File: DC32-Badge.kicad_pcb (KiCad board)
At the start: 2 copper layers, 152.4 x 101.6 mm, 55 parts, among them J1 Conn_01x06, J2 Hirose_FH34-SRJ-24S, J3 Conn_01x06, J4 Conn_01x06, J5 Conn_01x06, J6 Micro_SD_Card_Det, P1 2479, Q1 RTF025N03TL, SW1 SW_Push_DPDT, SW2 EVIL_SWITCH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

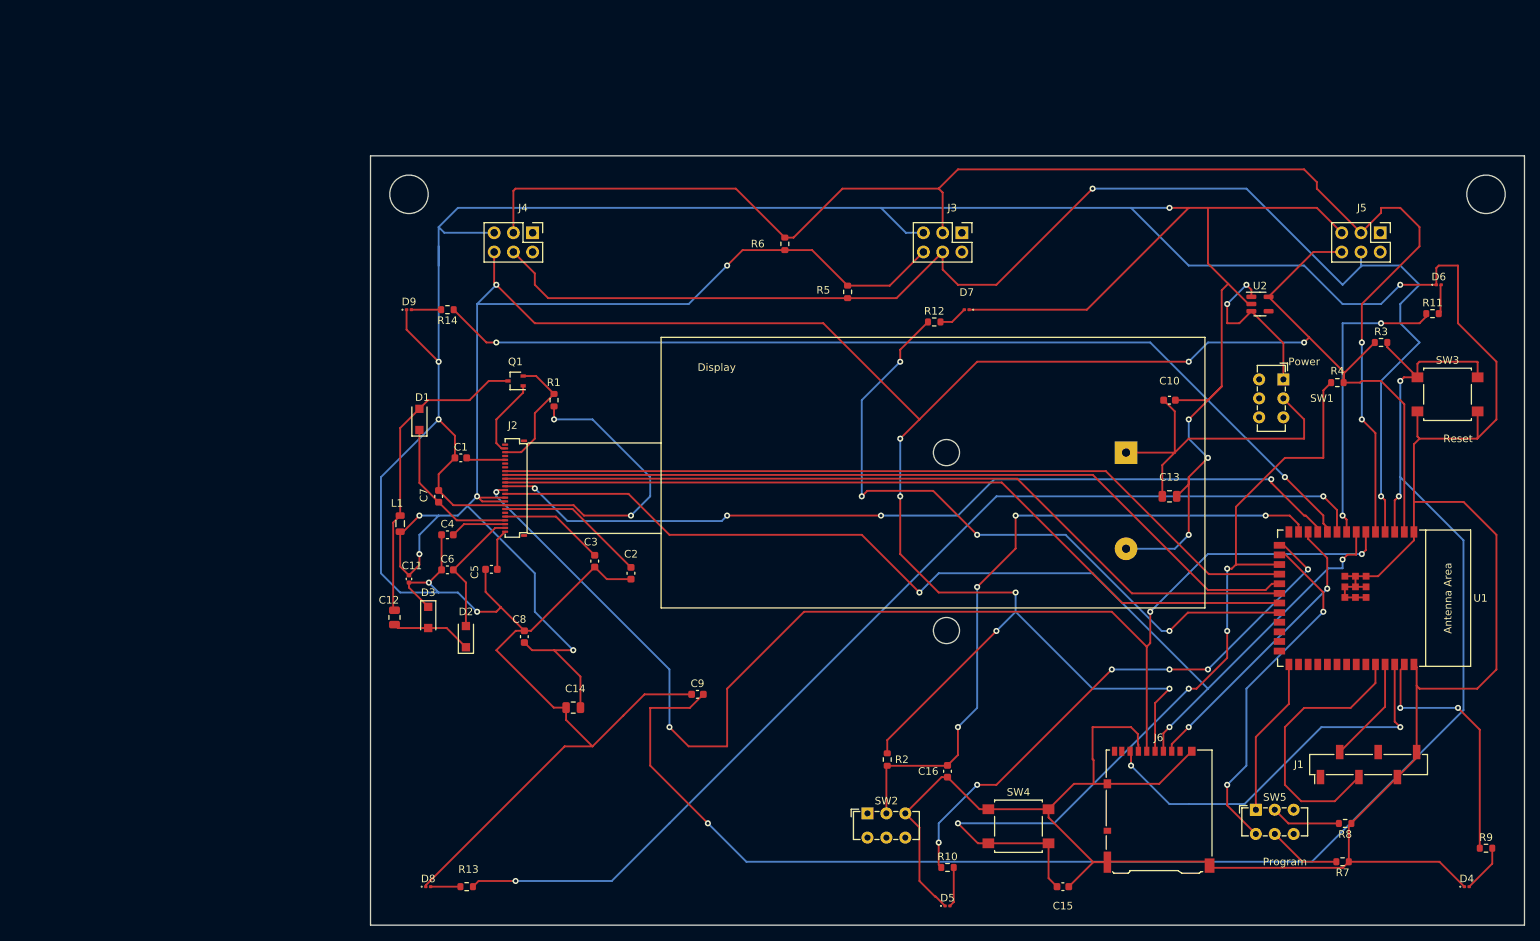
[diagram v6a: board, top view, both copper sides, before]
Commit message: Updated silkscreen.
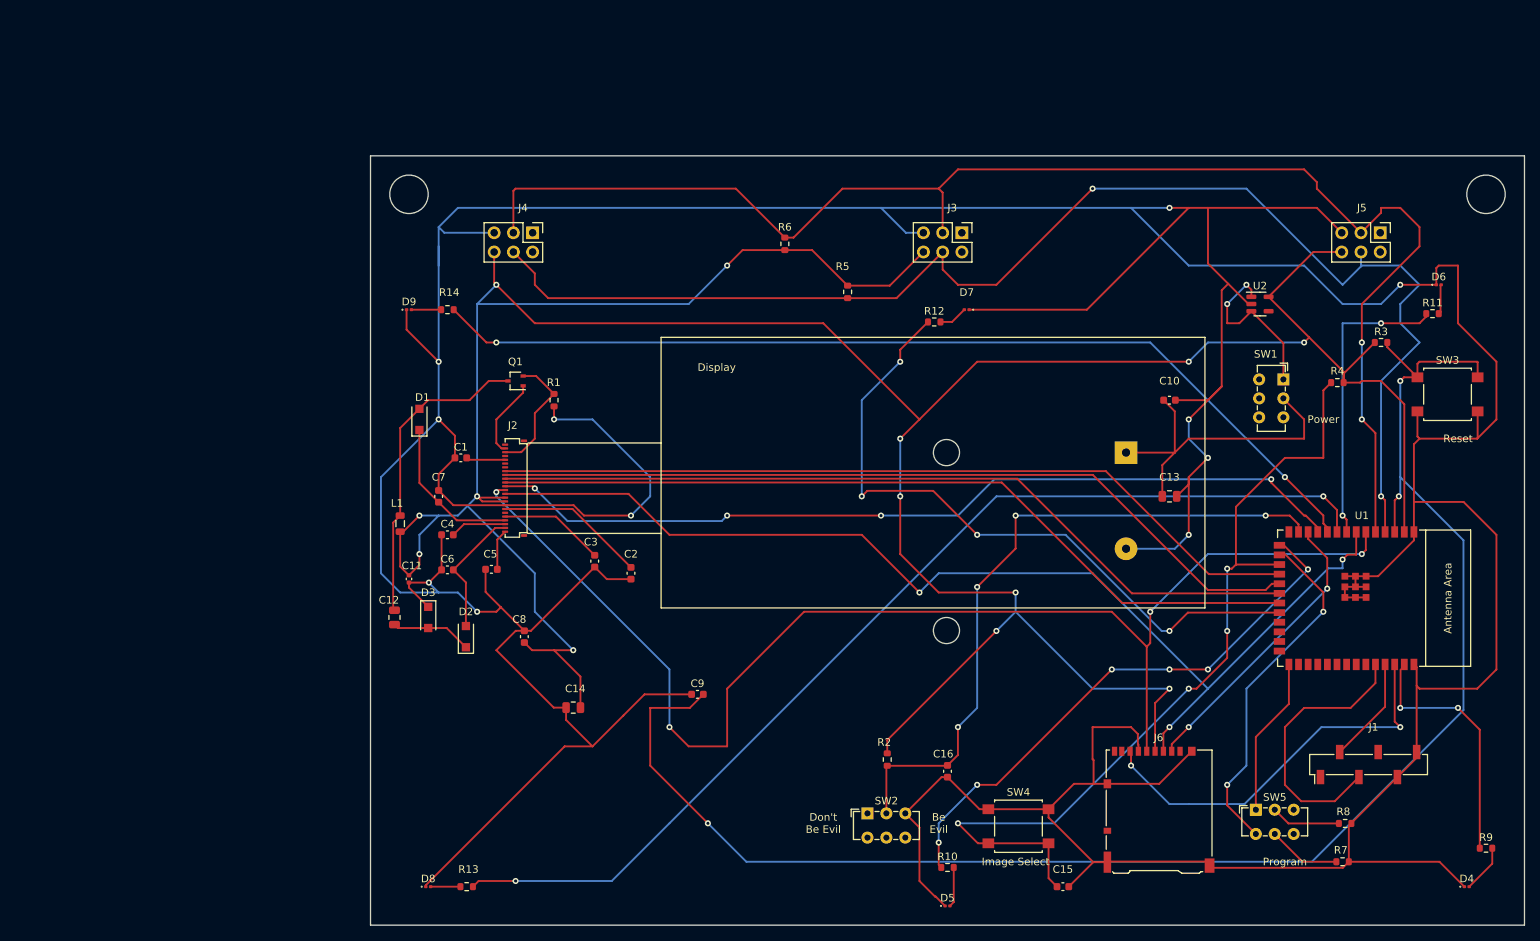
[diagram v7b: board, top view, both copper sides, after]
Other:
- board text added: "Be Evil"
- board text added: "Don't Be Evil"
- board text added: "Image Select"
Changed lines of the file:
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@@
     (property "Sheetname" "")
     (attr smd)
-    (fp_text reference "R7" (at 0 -1.43) (layer "F.SilkS")
+    (fp_text reference "R7" (at 0.237258 1.54) (layer "F.SilkS")
       (effects (font (size 1 1) (thickness 0.15)))
     )
@@
     (property "Sheetname" "")
     (attr smd)
-    (fp_text reference "R5" (at -0.237258 3.21) (layer "F.SilkS")
+    (fp_text reference "R5" (at -3.36 0.67) (layer "F.SilkS")
       (effects (font (size 1 1) (thickness 0.15)))
     )
@@
     (property "Sheetname" "")
     (attr smd)
-    (fp_text reference "C5" (at -2.22 0.35129 90) (layer "F.SilkS")
+    (fp_text reference "C5" (at -0.14058 -2.02 180) (layer "F.SilkS")
       (effects (font (size 1 1) (thickness 0.15)))
     )
@@
     (property "Sheetname" "")
     (attr smd)
-    (fp_text reference "C16" (at 0 -2.54 180) (layer "F.SilkS")
+    (fp_text reference "C16" (at 2.29 -0.56129 180) (layer "F.SilkS")
       (effects (font (size 1 1) (thickness 0.15)))
     )
@@
     (property "Sheetname" "")
     (attr through_hole)
-    (fp_text reference "SW1" (at 2.5 -5.08 180) (layer "F.SilkS")
+    (fp_text reference "SW1" (at -3.34 2.34129 180) (layer "F.SilkS")
       (effects (font (size 1 1) (thickness 0.15)))
     )
@@
     (property "Sheetname" "")
     (attr smd)
-    (fp_text reference "R6" (at 0 -3.577258) (layer "F.SilkS")
+    (fp_text reference "R6" (at 2.214516 0) (layer "F.SilkS")
       (effects (font (size 1 1) (thickness 0.15)))
     )
@@
     (property "Sheetname" "")
     (attr smd)
-    (fp_text reference "C15" (at 0 -2.54) (layer "F.SilkS")
+    (fp_text reference "C15" (at 0 2.29) (layer "F.SilkS")
       (effects (font (size 1 1) (thickness 0.15)))
     )
@@
     (property "Sheetname" "")
     (attr smd)
-    (fp_text reference "U1" (at 0 -17.05 180) (layer "F.SilkS")
+    (fp_text reference "U1" (at -10.91 -1.37871 180) (layer "F.SilkS")
       (effects (font (size 1 1) (thickness 0.15)))
     )
@@
     (property "Sheetname" "")
     (attr smd)
-    (fp_text reference "C7" (at -0.14058 1.96 -270) (layer "F.SilkS")
+    (fp_text reference "C7" (at -2.54 0 -180) (layer "F.SilkS")
       (effects (font (size 1 1) (thickness 0.15)))
     )
@@
     (property "Sheetname" "")
     (attr smd)
-    (fp_text reference "R2" (at 0 -1.93 180) (layer "F.SilkS")
+    (fp_text reference "R2" (at -2.28 0.405 180) (layer "F.SilkS")
       (effects (font (size 1 1) (thickness 0.15)))
     )
@@
     (property "Sheetname" "")
     (attr smd)
-    (fp_text reference "J1" (at 0 -9.22 180) (layer "F.SilkS")
+    (fp_text reference "J1" (at 4.94 0.64871 180) (layer "F.SilkS")
       (effects (font (size 1 1) (thickness 0.15)))
     )
@@
     (property "Sheetname" "")
     (attr smd)
-    (fp_text reference "R8" (at 0 -1.43) (layer "F.SilkS")
+    (fp_text reference "R8" (at 0.237258 1.56) (layer "F.SilkS")
       (effects (font (size 1 1) (thickness 0.15)))
     )
@@
     (property "Sheetname" "")
     (attr smd)
-    (fp_text reference "R14" (at 0 -1.43) (layer "F.SilkS")
+    (fp_text reference "R14" (at -0.237258 2.29) (layer "F.SilkS")
       (effects (font (size 1 1) (thickness 0.15)))
     )
@@
   (gr_rect (start 77.36129 41.39) (end 229.76129 142.99) (layer "Edge.Cuts") (width 0.1) (fill none))
   (gr_circle (center 82.44129 46.47) (end 84.98129 46.47) (layer "Edge.Cuts") (width 0.1) (fill none))
-  (gr_text "Power\n" (at 200.66 68.58) (layer "F.SilkS")
+  (gr_text "Image Select" (at 162.56 134.62) (layer "F.SilkS")
+    (effects (font (size 1 1) (thickness 0.15)))
+  )
+  (gr_text "Power\n" (at 203.2 76.2) (layer "F.SilkS")
     (effects (font (size 1 1) (thickness 0.15)))
   )
@@
     (effects (font (size 1 1) (thickness 0.15)))
   )
+  (gr_text "Don't \nBe Evil" (at 137.16 129.54) (layer "F.SilkS")
+    (effects (font (size 1 1) (thickness 0.15)))
+  )
+  (gr_text "Be \nEvil" (at 152.4 129.54) (layer "F.SilkS")
+    (effects (font (size 1 1) (thickness 0.15)))
+  )
